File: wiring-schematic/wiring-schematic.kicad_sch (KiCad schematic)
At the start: 6 parts, among them U0 LSM9DS1, U1 LSM9DS1, U2 LSM9DS1, U3 LSM9DS1, U4 LSM9DS1

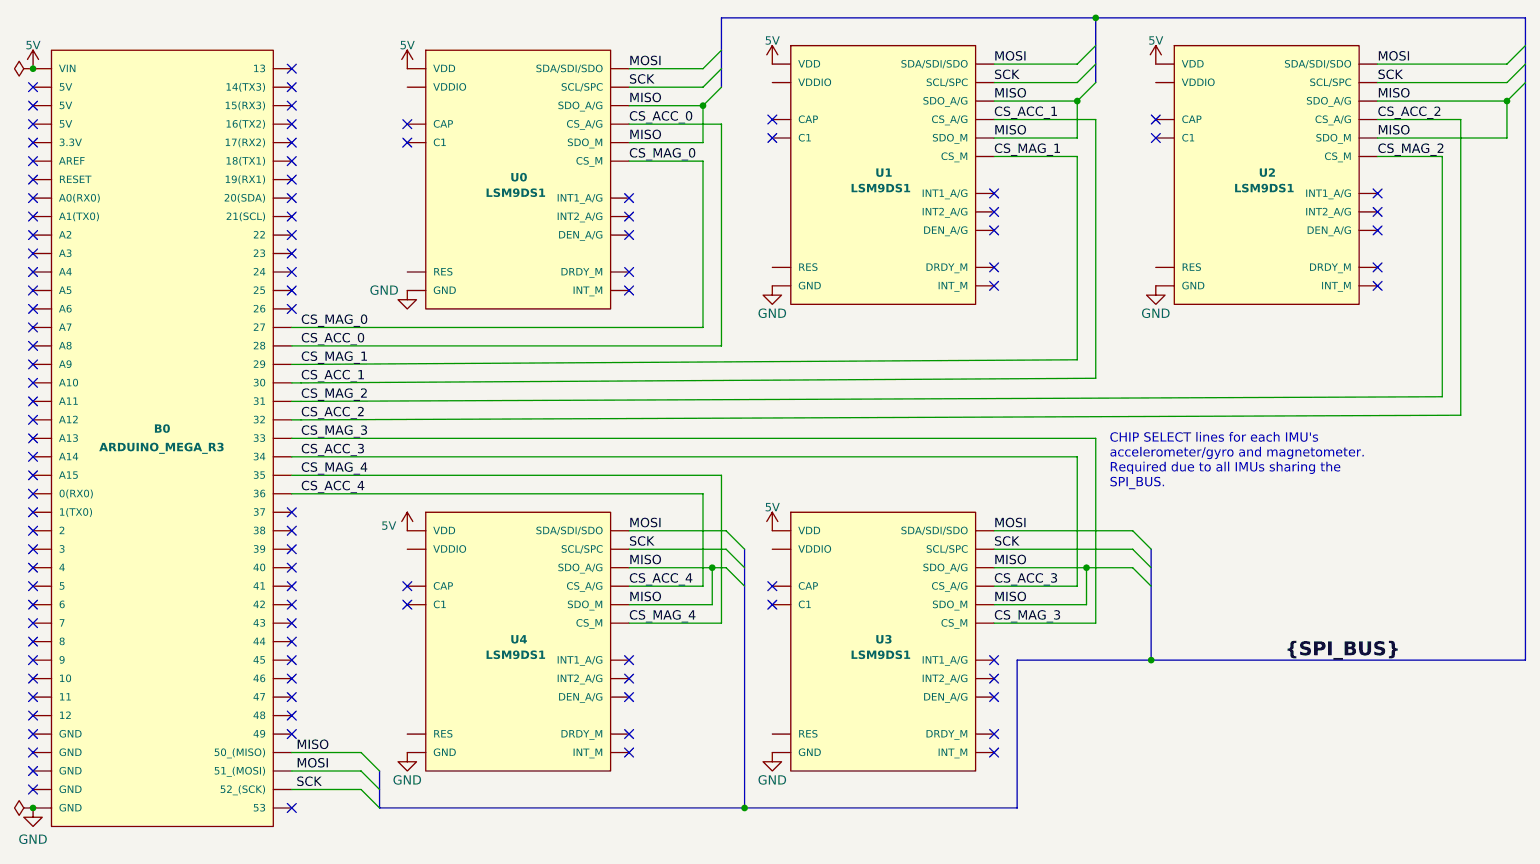
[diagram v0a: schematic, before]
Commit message: Updated KiCad schematic to use Raspberry Pi. TODO: update readme for RPi wiringdetails
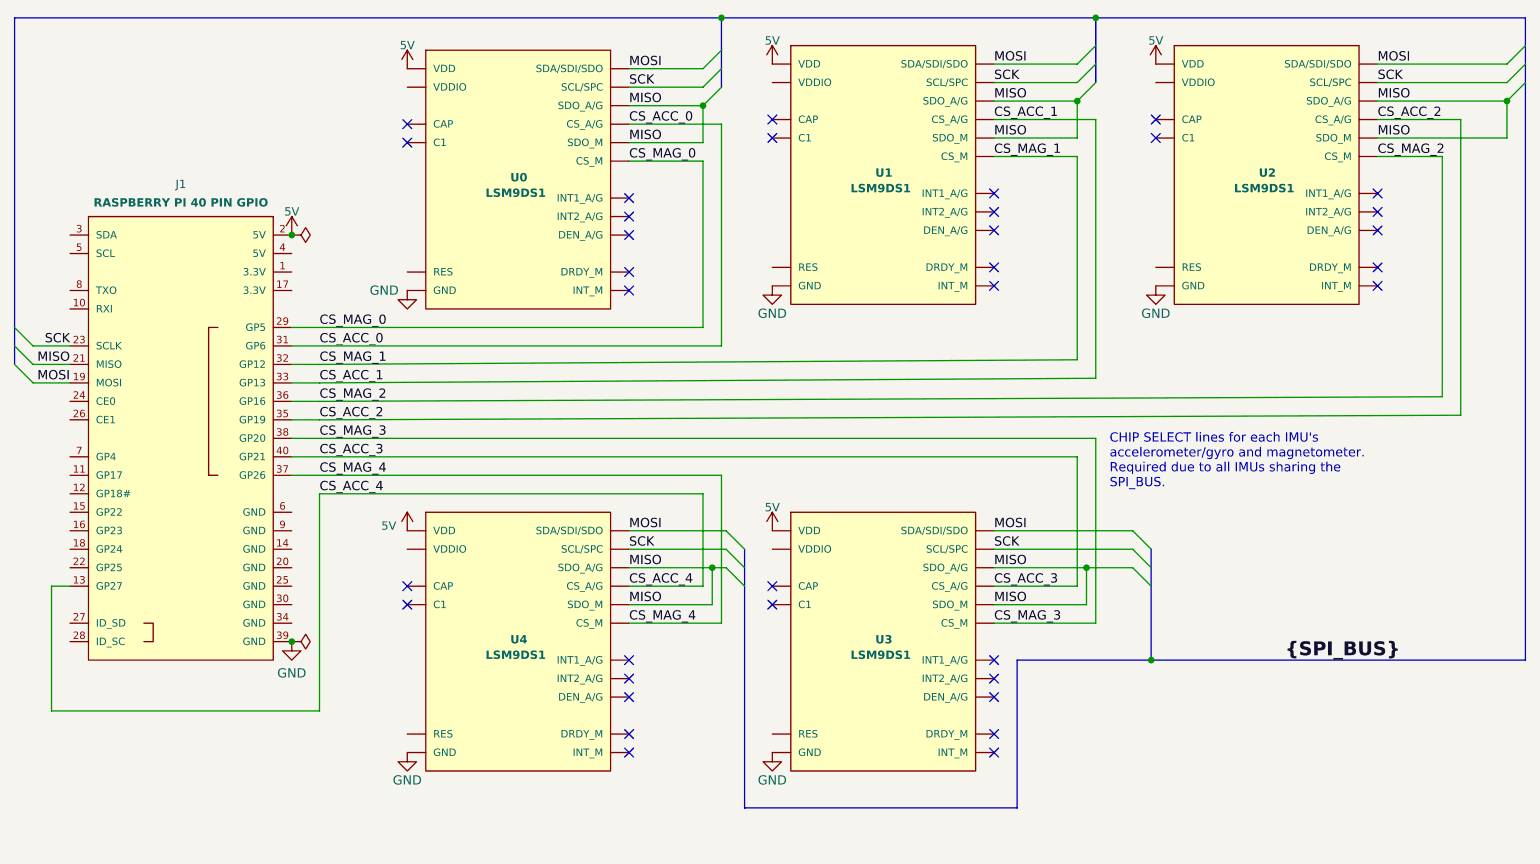
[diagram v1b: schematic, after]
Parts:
- removed B0: ARDUINO_MEGA_R3, ARDUINO_MEGA, symbol SparkFun-Boards:ARDUINO_MEGA_R3FULL
- added J1: RASPBERRY PI 40 PIN GPIO, SparkFun-Connectors:2X20, symbol SparkFun-Connectors:RASPBERRYPI-40-PIN-GPIO_PTH_NO_SHROUD
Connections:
- net 5V: now also J1.2 (5V)
- net CS_ACC_0: now also J1.31 (GP6)
- net CS_ACC_1: now also J1.33 (GP13)
- net CS_ACC_2: now also J1.35 (GP19)
- net CS_ACC_3: now also J1.40 (GP21)
- net CS_ACC_4: now also J1.13 (GP27)
- net CS_MAG_0: now also J1.29 (GP5)
- net CS_MAG_1: now also J1.32 (GP12)
- net CS_MAG_2: now also J1.36 (GP16)
- net CS_MAG_3: now also J1.38 (GP20)
- net CS_MAG_4: now also J1.37 (GP26)
- net GND: now also J1.39 (GND)
- net MISO: now also J1.21 (MISO)
- net MOSI: now also J1.19 (MOSI)
- net SCK: now also J1.23 (SCLK)
- no-connect marks 102 -> 35
